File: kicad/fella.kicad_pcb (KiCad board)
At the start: 2 copper layers, 44 parts, among them J2 DE15_Receptacle_HighDensity_M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, SW1 SW_MEC_5E, U1 74HC163, U10 TMS4416, U11 TMS4416, U12 TMS4416, U13 74HC157, U14 74HC157, U15 74HC04, U16 74HC32, U17 74HC174, U18 XC9536PC44, U2 NE555P, U22 74HC02, U24 6264, U25 74HC574, U26 2764, U27 74HC166, U4 W65C02SxP, U5 27128, U8 CY62256-70PC, U9 TMS4416, X1 ACO-25.175MHz-A

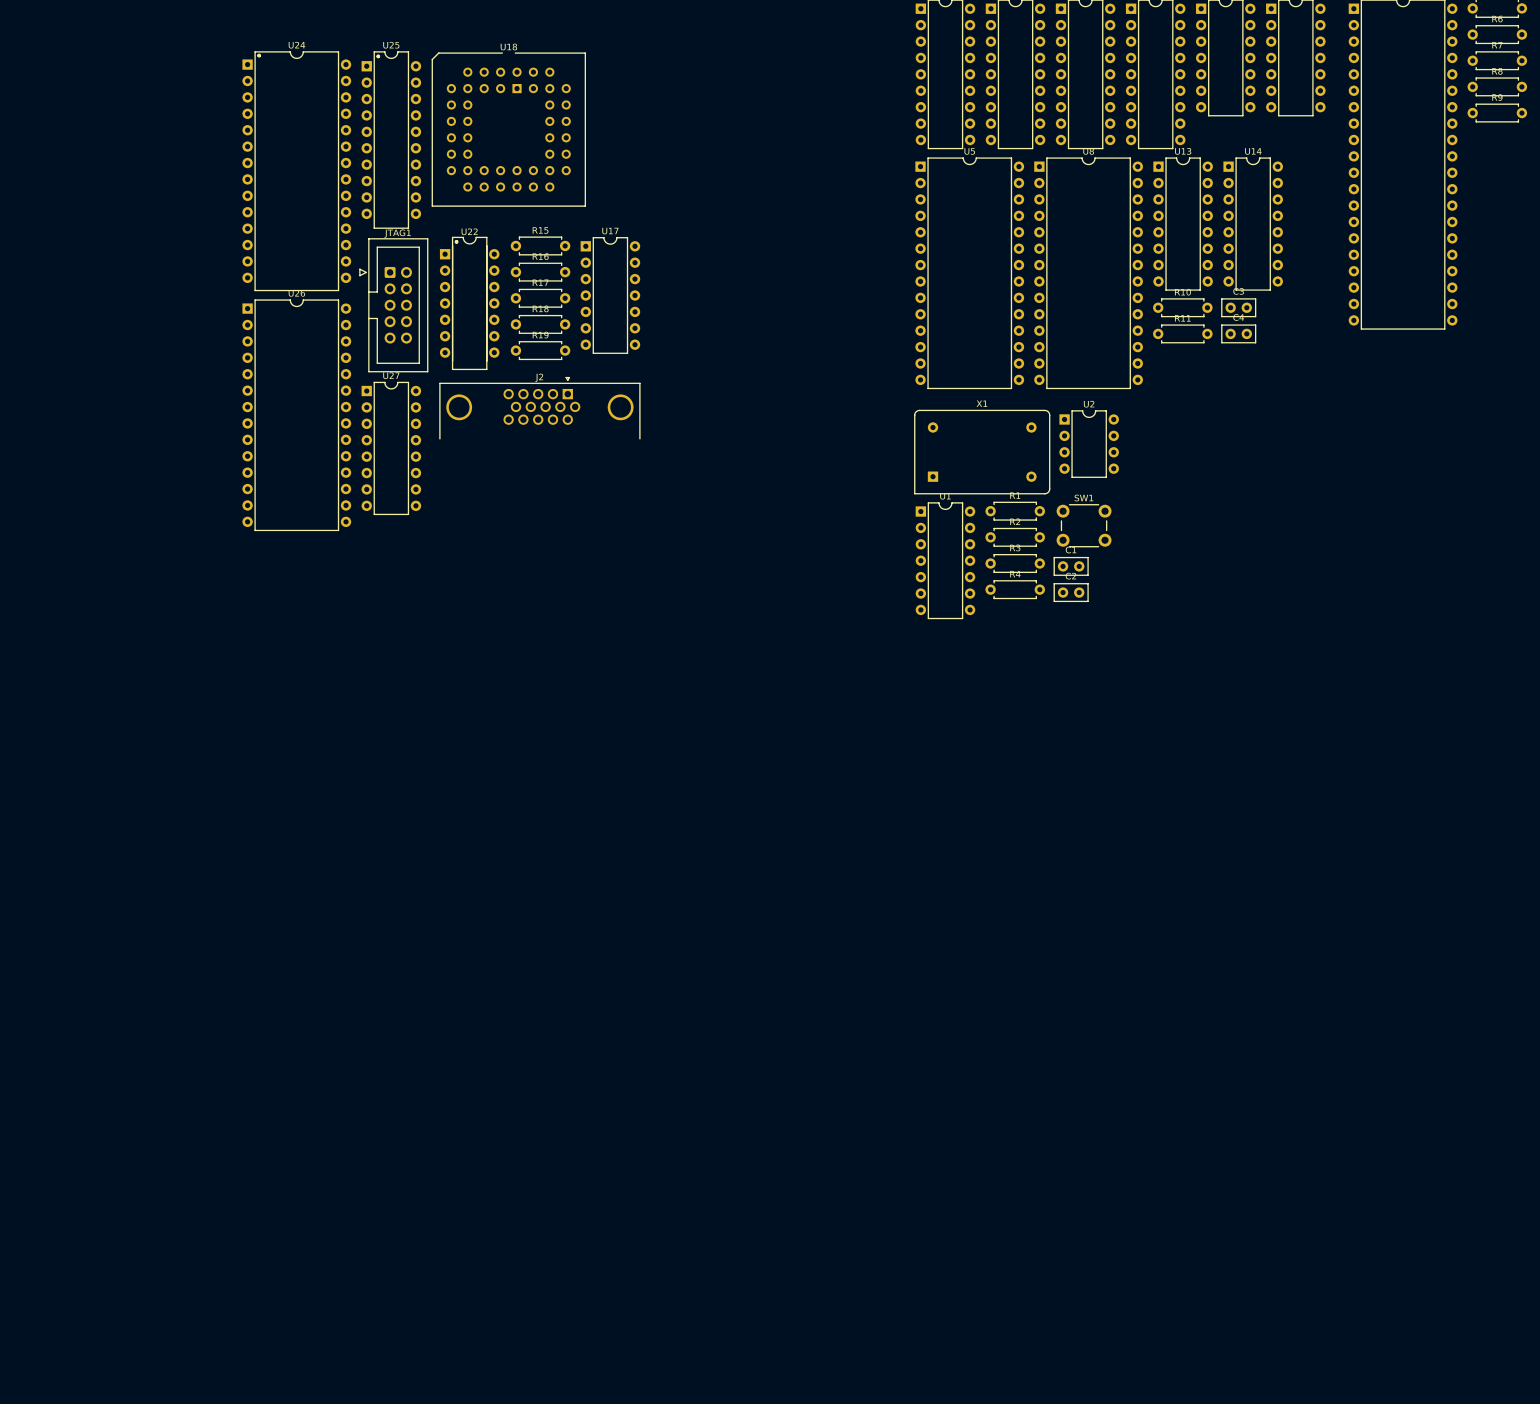
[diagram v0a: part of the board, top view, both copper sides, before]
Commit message: Add user IO and USB
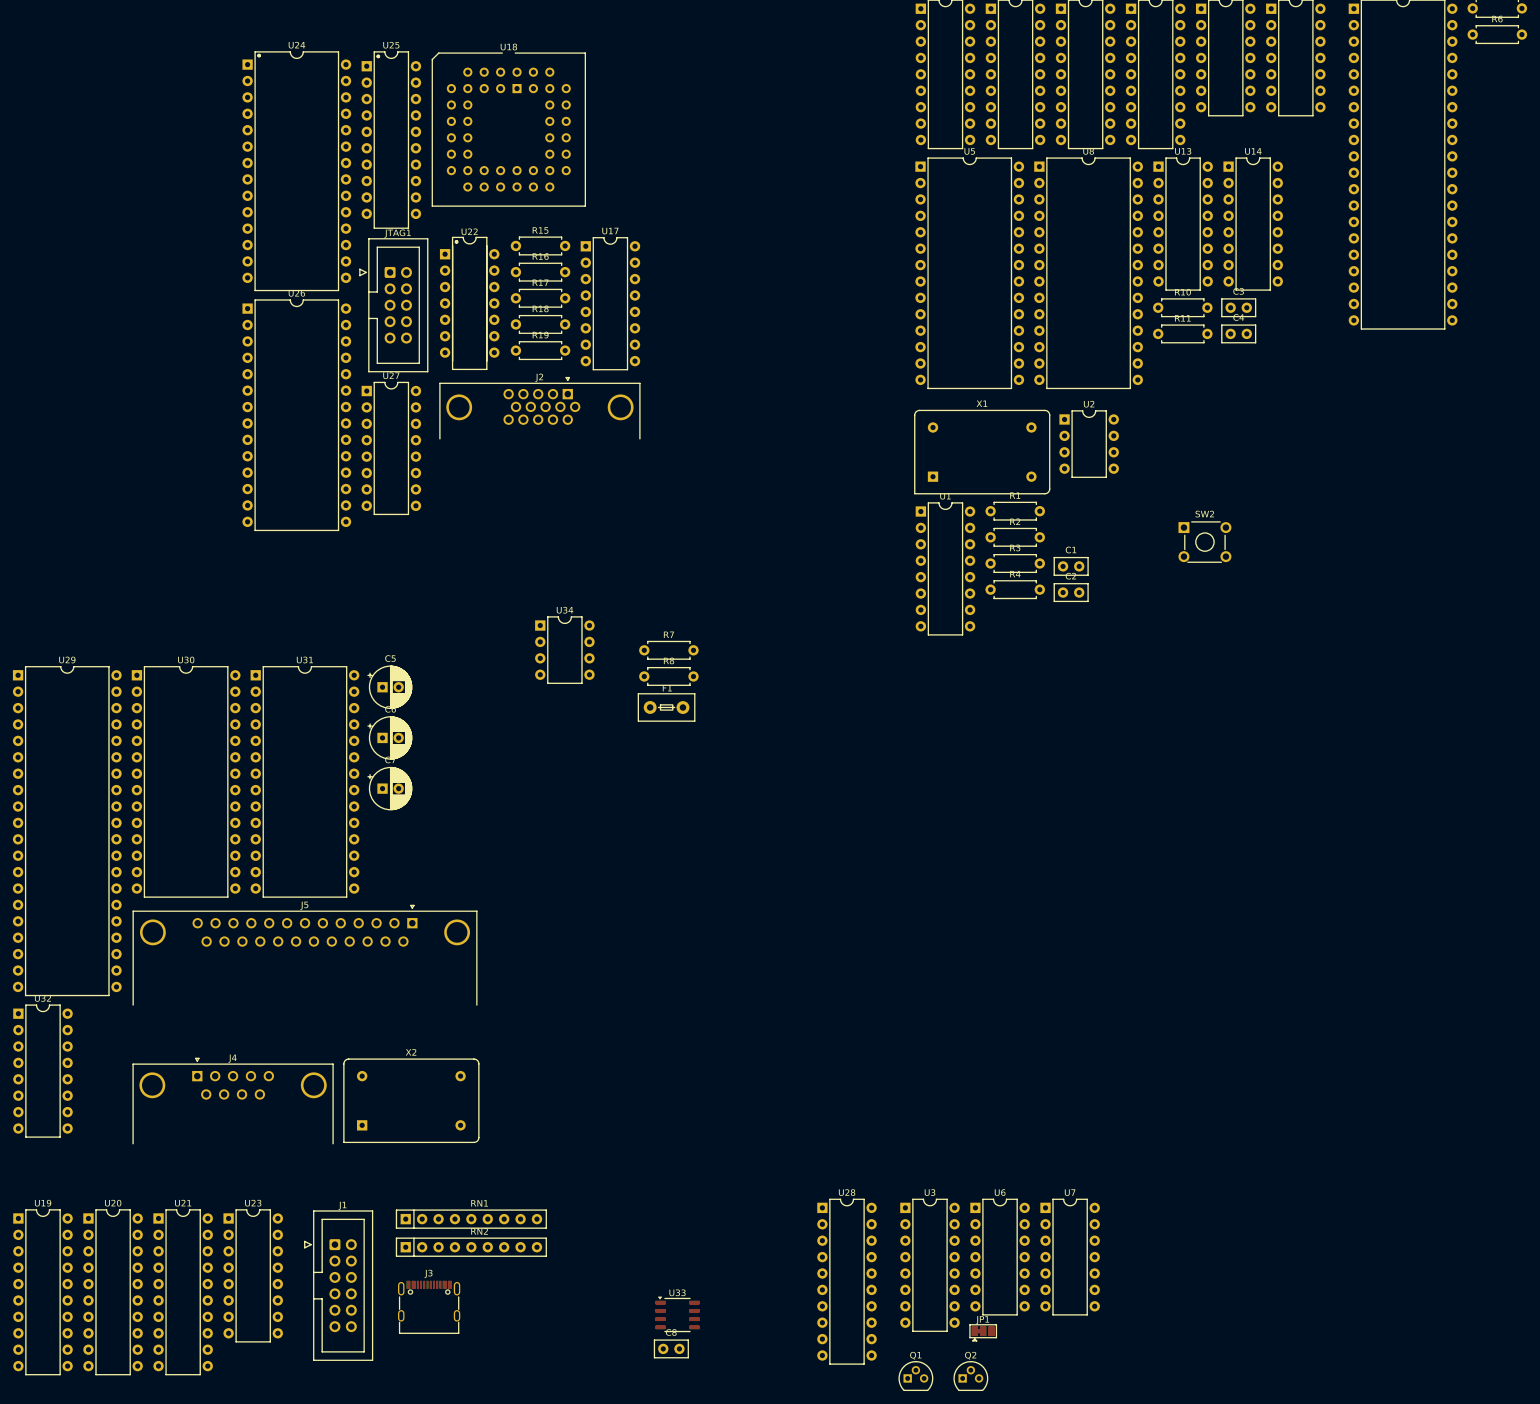
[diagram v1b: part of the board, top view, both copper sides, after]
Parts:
- removed R9: 10K, Resistor_THT:R_Axial_DIN0207_L6.3mm_D2.5mm_P7.62mm_Horizontal
- removed SW1: SW_MEC_5E, Button_Switch_THT:SW_PUSH_6mm_H4.3mm
- added C5: 10u, Capacitor_THT:CP_Radial_D6.3mm_P2.50mm, F.Cu at (-56.2, 139.1)
- added C6: 10u, Capacitor_THT:CP_Radial_D6.3mm_P2.50mm, F.Cu at (-56.2, 146.9)
- added C7: 10u, Capacitor_THT:CP_Radial_D6.3mm_P2.50mm, F.Cu at (-56.2, 154.8)
- added C8: 100n, Capacitor_THT:C_Disc_D5.0mm_W2.5mm_P2.50mm, F.Cu at (-12.7, 241.6)
- added F1: Fuse, PCM_Fuse_AKL:Fuse_Littelfuse_395Series, F.Cu at (-14.7, 142.2)
- added J1: Conn_02x06_Odd_Even, Connector_IDC:IDC-Header_2x06_P2.54mm_Vertical, F.Cu at (-63.5, 225.4)
- added J3: USB_C_Receptacle_USB2.0_14P, Connector_USB:USB_C_Receptacle_G-Switch_GT-USB-7010ASV, F.Cu at (-49.0, 235.4)
- added J4: DE9_Plug_MountingHoles, Connector_Dsub:DSUB-9_Male_Horizontal_P2.77x2.84mm_EdgePinOffset7.70mm_Housed_MountingHolesOffset9.12mm, F.Cu at (-84.9, 199.3)
- added J5: DB25_Receptacle_MountingHoles, Connector_Dsub:DSUB-25_Female_Horizontal_P2.77x2.84mm_EdgePinOffset9.90mm_Housed_MountingHolesOffset11.32mm, F.Cu at (-51.6, 175.6)
- added JP1: Jumper_3_Bridged12, Jumper:SolderJumper-3_P1.3mm_Bridged12_Pad1.0x1.5mm, F.Cu at (36.8, 238.8)
- added Q1: BC547, Package_TO_SOT_THT:TO-92, F.Cu at (25.1, 246.1)
- added Q2: BC547, Package_TO_SOT_THT:TO-92, F.Cu at (33.7, 246.1)
- added RN1: 4K7x8, Resistor_THT:R_Array_SIP9, F.Cu at (-52.6, 221.5)
- added RN2: 10Kx8, Resistor_THT:R_Array_SIP9, F.Cu at (-52.6, 225.8)
- added SW2: SW_Omron_B3FS, Button_Switch_THT:SW_TH_Tactile_Omron_B3F-10xx, F.Cu at (67.9, 114.4)
- added U19: 74HC574, Package_DIP:DIP-20_W7.62mm, F.Cu at (-112.6, 221.4)
- added U20: 74HC574, Package_DIP:DIP-20_W7.62mm, F.Cu at (-101.7, 221.4)
- added U21: 74HC245, Package_DIP:DIP-20_W7.62mm, F.Cu at (-90.9, 221.4)
- added U23: 74HC138, Package_DIP:DIP-16_W7.62mm, F.Cu at (-80.0, 221.4)
- added U28: 74HC244, Package_DIP:DIP-20_W7.62mm, F.Cu at (11.9, 219.7)
- added U29: 6522, Package_DIP:DIP-40_W15.24mm, F.Cu at (-112.6, 137.2)
- added U3: 74HC138, Package_DIP:DIP-16_W7.62mm, F.Cu at (24.8, 219.7)
- added U30: 6551, Package_DIP:DIP-28_W15.24mm, F.Cu at (-94.2, 137.2)
- added U31: 6551, Package_DIP:DIP-28_W15.24mm, F.Cu at (-75.8, 137.2)
- added U32: MAX232, Package_DIP:DIP-16_W7.62mm, F.Cu at (-112.6, 189.6)
- added U33: CH340N, Package_SO:SOP-8_3.9x4.9mm_P1.27mm, F.Cu at (-10.5, 236.3)
- added U34: 24LC256, Package_DIP:DIP-8_W7.62mm, F.Cu at (-31.8, 129.5)
- added U6: 74HC04, Package_DIP:DIP-14_W7.62mm, F.Cu at (35.6, 219.7)
- added U7: 74HC00, Package_DIP:DIP-14_W7.62mm, F.Cu at (46.5, 219.7)
- added X2: ACO-1.8432MHz-A, Oscillator:Oscillator_DIP-14, F.Cu at (-59.3, 206.9)
- R7, R8: value 10K -> 4K7
- U1, U17: footprint Package_DIP:DIP-14_W7.62mm -> Package_DIP:DIP-16_W7.62mm
- moved R7 157.4 mm to (-15.6, 133.4)
- moved R8 157.4 mm to (-15.6, 137.4)
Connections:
- net Net-(U17-Q0) renamed /vga/~{BLANK}
- net Net-(U17-Q2) renamed /vga/HSYNC
- net Net-(U17-Q3) renamed /vga/~{LOAD}
- R19 pad 1: Net-(U17-Q1) -> /vga/VSYNC
- R5 pad 1: VCC -> Net-(J3-CC2)
- R5 pad 2: /cpu//IRQ -> GND
- R6 pad 1: VCC -> Net-(J3-CC1)
- R6 pad 2: /cpu//NMI -> GND
- R7 pad 1: VCC -> Net-(U29-PB7)
- R7 pad 2: Net-(U4-RDY) -> VCC
- R8 pad 1: VCC -> Net-(U29-PB6)
- R8 pad 2: Net-(U4-BE) -> VCC
- U17 pad 5: Net-(U17-Q1) -> /vga/VSYNC
- U22 pad 4: unconnected-(U22-Pad4) -> /cpu//NMI
- U22 pad 5: GND -> /vga/VSYNC
- U22 pad 6: GND -> /vga/VSYNC
- U4 pad 2: Net-(U4-RDY) -> Net-(RN2-R3)
- U4 pad 36: Net-(U4-BE) -> Net-(RN2-R2)

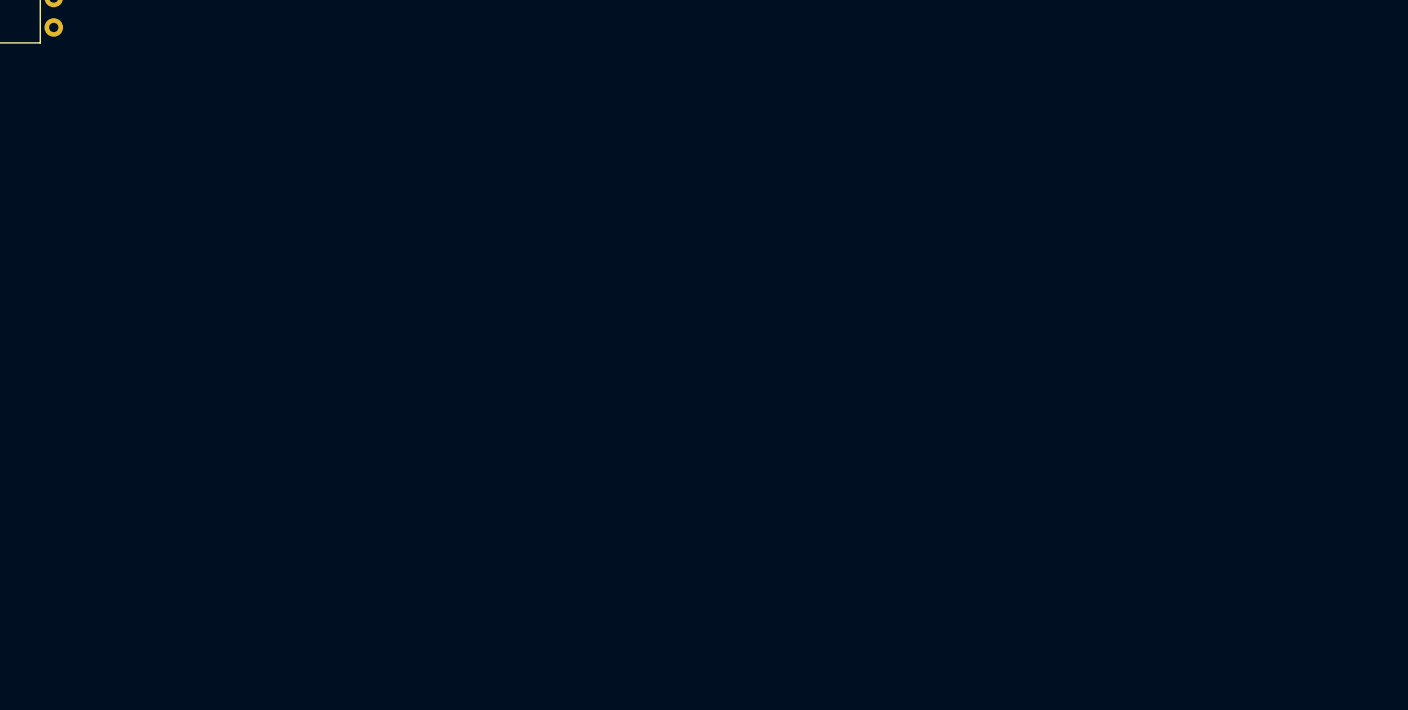
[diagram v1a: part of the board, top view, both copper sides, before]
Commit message: Add expansion slot
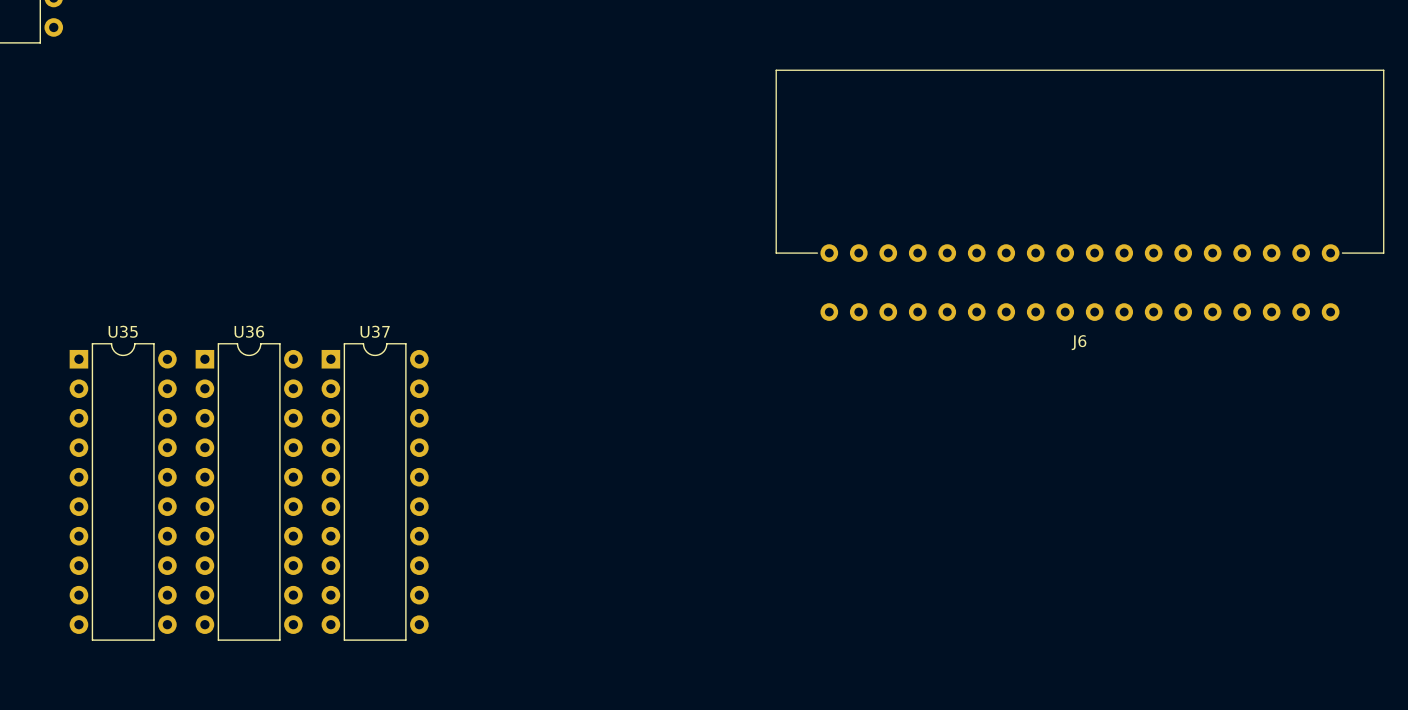
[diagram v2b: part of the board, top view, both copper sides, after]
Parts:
- added J6: Conn_02x18_Top_Bottom, 8bits:EDGE_2x18, F.Cu at (123.2, 151.6)
- added U35: 74HC244, Package_DIP:DIP-20_W7.62mm, F.Cu at (37.0, 158.2)
- added U36: 74HC244, Package_DIP:DIP-20_W7.62mm, F.Cu at (47.8, 158.2)
- added U37: 74HC245, Package_DIP:DIP-20_W7.62mm, F.Cu at (58.7, 158.2)

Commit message: Add caps and make initial placement
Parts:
- added C10: 100n, Capacitor_THT:C_Disc_D5.0mm_W2.5mm_P2.50mm, F.Cu at (109.2, -83.8)
- added C11: 100n, Capacitor_THT:C_Disc_D5.0mm_W2.5mm_P2.50mm, F.Cu at (109.2, -101.6)
- added C12: 100n, Capacitor_THT:C_Disc_D5.0mm_W2.5mm_P2.50mm, F.Cu at (64.8, -144.8)
- added C13: 100n, Capacitor_THT:C_Disc_D5.0mm_W2.5mm_P2.50mm, F.Cu at (62.3, -110.5)
- added C14: 100n, Capacitor_THT:C_Disc_D5.0mm_W2.5mm_P2.50mm, F.Cu at (177.8, -92.7)
- added C15: 100n, Capacitor_THT:C_Disc_D5.0mm_W2.5mm_P2.50mm, F.Cu at (130.8, -82.5)
- added C16: 100n, Capacitor_THT:C_Disc_D5.0mm_W2.5mm_P2.50mm, F.Cu at (317.5, -102.9)
- added C17: 100n, Capacitor_THT:C_Disc_D5.0mm_W2.5mm_P2.50mm, F.Cu at (329.0, -102.9)
- added C18: 100n, Capacitor_THT:C_Disc_D5.0mm_W2.5mm_P2.50mm, F.Cu at (313.7, -125.7)
- added C19: 100n, Capacitor_THT:C_Disc_D5.0mm_W2.5mm_P2.50mm, F.Cu at (304.8, -137.2)
- added C20: 100n, Capacitor_THT:C_Disc_D5.0mm_W2.5mm_P2.50mm, F.Cu at (278.2, -141.0)
- added C21: 100n, Capacitor_THT:C_Disc_D5.0mm_W2.5mm_P2.50mm, F.Cu at (223.5, -86.3)
- added C22: 100n, Capacitor_THT:C_Disc_D5.0mm_W2.5mm_P2.50mm, F.Cu at (274.3, -100.3)
- added C23: 100n, Capacitor_THT:C_Disc_D5.0mm_W2.5mm_P2.50mm, F.Cu at (285.8, -99.1)
- added C24: 100n, Capacitor_THT:C_Disc_D5.0mm_W2.5mm_P2.50mm, F.Cu at (294.7, -102.9)
- added C25: 100n, Capacitor_THT:C_Disc_D5.0mm_W2.5mm_P2.50mm, F.Cu at (306.1, -102.9)
- added C26: 100n, Capacitor_THT:C_Disc_D5.0mm_W2.5mm_P2.50mm, F.Cu at (177.8, -106.7)
- added C27: 100n, Capacitor_THT:C_Disc_D5.0mm_W2.5mm_P2.50mm, F.Cu at (219.7, -132.1)
- added C28: 100n, Capacitor_THT:C_Disc_D5.0mm_W2.5mm_P2.50mm, F.Cu at (137.2, -139.7)
- added C29: 100n, Capacitor_THT:C_Disc_D5.0mm_W2.5mm_P2.50mm, F.Cu at (104.2, -151.1)
- added C30: 100n, Capacitor_THT:C_Disc_D5.0mm_W2.5mm_P2.50mm, F.Cu at (219.7, -147.3)
- added C31: 100n, Capacitor_THT:C_Disc_D5.0mm_W2.5mm_P2.50mm, F.Cu at (105.4, -105.4)
- added C32: 100n, Capacitor_THT:C_Disc_D5.0mm_W2.5mm_P2.50mm, F.Cu at (329.0, -125.7)
- added C33: 100n, Capacitor_THT:C_Disc_D5.0mm_W2.5mm_P2.50mm, F.Cu at (278.1, -113.0)
- added C34: 100n, Capacitor_THT:C_Disc_D5.0mm_W2.5mm_P2.50mm, F.Cu at (121.9, -120.7)
- added C35: 100n, Capacitor_THT:C_Disc_D5.0mm_W2.5mm_P2.50mm, F.Cu at (105.4, -139.7)
- added C36: 100n, Capacitor_THT:C_Disc_D5.0mm_W2.5mm_P2.50mm, F.Cu at (78.8, -151.1)
- added C37: 100n, Capacitor_THT:C_Disc_D5.0mm_W2.5mm_P2.50mm, F.Cu at (67.3, -139.7)
- added C38: 100n, Capacitor_THT:C_Disc_D5.0mm_W2.5mm_P2.50mm, F.Cu at (219.7, -111.7)
- added C39: 100n, Capacitor_THT:C_Disc_D5.0mm_W2.5mm_P2.50mm, F.Cu at (219.7, -115.6)
- added C40: 100n, Capacitor_THT:C_Disc_D5.0mm_W2.5mm_P2.50mm, F.Cu at (92.7, -139.7)
- added C41: 100n, Capacitor_THT:C_Disc_D5.0mm_W2.5mm_P2.50mm, F.Cu at (132.1, -155.0)
- added C42: 100n, Capacitor_THT:C_Disc_D5.0mm_W2.5mm_P2.50mm, F.Cu at (177.8, -146.0)
- added C43: 100n, Capacitor_THT:C_Disc_D5.0mm_W2.5mm_P2.50mm, F.Cu at (179.1, -152.4)
- added C44: 100n, Capacitor_THT:C_Disc_D5.0mm_W2.5mm_P2.50mm, F.Cu at (80.0, -139.7)
- added C45: 100n, Capacitor_THT:C_Disc_D5.0mm_W2.5mm_P2.50mm, F.Cu at (271.8, -125.7)
- added C46: 100n, Capacitor_THT:C_Disc_D5.0mm_W2.5mm_P2.50mm, F.Cu at (80.0, -108.0)
- added C47: 100n, Capacitor_THT:C_Disc_D5.0mm_W2.5mm_P2.50mm, F.Cu at (137.2, -108.0)
- added C48: 470u, Capacitor_THT:CP_Radial_D10.0mm_P5.00mm, F.Cu at (96.4, -161.1)
- added C49: 470u, Capacitor_THT:CP_Radial_D10.0mm_P5.00mm, F.Cu at (108.0, -161.1)
- added C9: 100n, Capacitor_THT:C_Disc_D5.0mm_W2.5mm_P2.50mm, F.Cu at (92.7, -105.4)
- JP1: moved to B.Cu
- moved J4 456.6 mm to (203.7, -154.6), turned to 180 degrees
- moved U32 443.8 mm to (184.2, -140.3), turned to 90 degrees
- moved J5 432.8 mm to (231.0, -152.1), turned to 180 degrees
- moved U29 428.7 mm to (223.5, -128.9), turned to 90 degrees
- moved U30 426.5 mm to (256.5, -105.4), turned to -90 degrees
- moved U31 423.0 mm to (256.5, -124.5), turned to -90 degrees
- moved RN1 416.4 mm to (228.6, -85.7)
- moved Q2 416.2 mm to (129.9, -158.8), turned to 90 degrees
- moved J3 414.5 mm to (69.4, -161.9), turned to 180 degrees
- moved U21 404.6 mm to (97.8, -136.5)
- moved U20 403.7 mm to (85.0, -136.5)
- moved U19 402.8 mm to (72.3, -136.5)
- moved C8 400.6 mm to (72.4, -149.9), turned to 90 degrees
- moved U23 399.5 mm to (82.6, -143.5), turned to 90 degrees
- moved U33 395.8 mm to (67.3, -151.8), turned to -90 degrees
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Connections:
- U6 pad 13: unconnected-(U6-Pad13) -> GND
- U7 pad 10: unconnected-(U7-Pad10) -> GND
- U7 pad 12: unconnected-(U7-Pad12) -> GND
- U7 pad 13: unconnected-(U7-Pad13) -> GND
- U7 pad 9: unconnected-(U7-Pad9) -> GND
